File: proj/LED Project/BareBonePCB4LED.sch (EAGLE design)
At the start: 12 parts, among them J3 AVR_SPI_PROG_3X2NS, Y1 16MHz

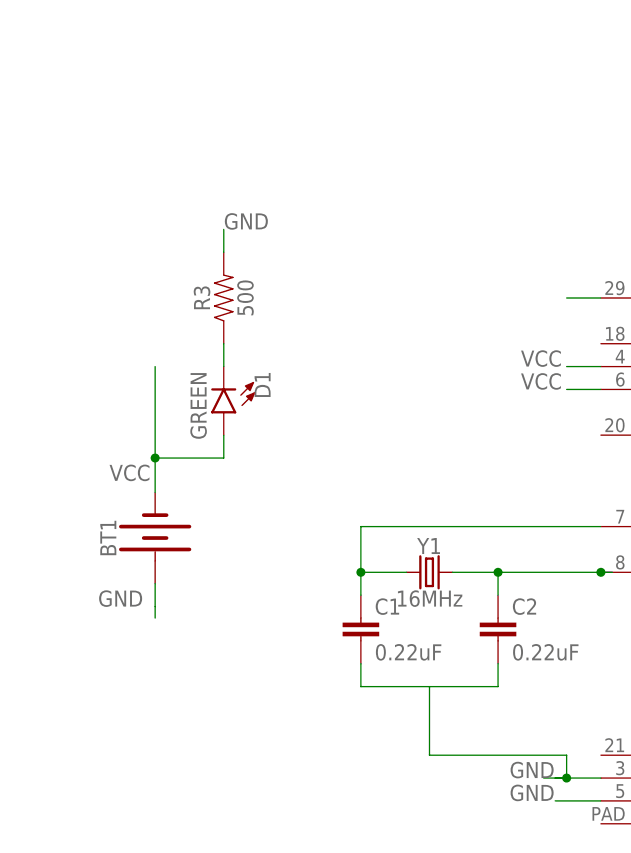
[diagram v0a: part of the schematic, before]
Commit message: Added volt regulator to bring battery from 9v to 5v for board tests
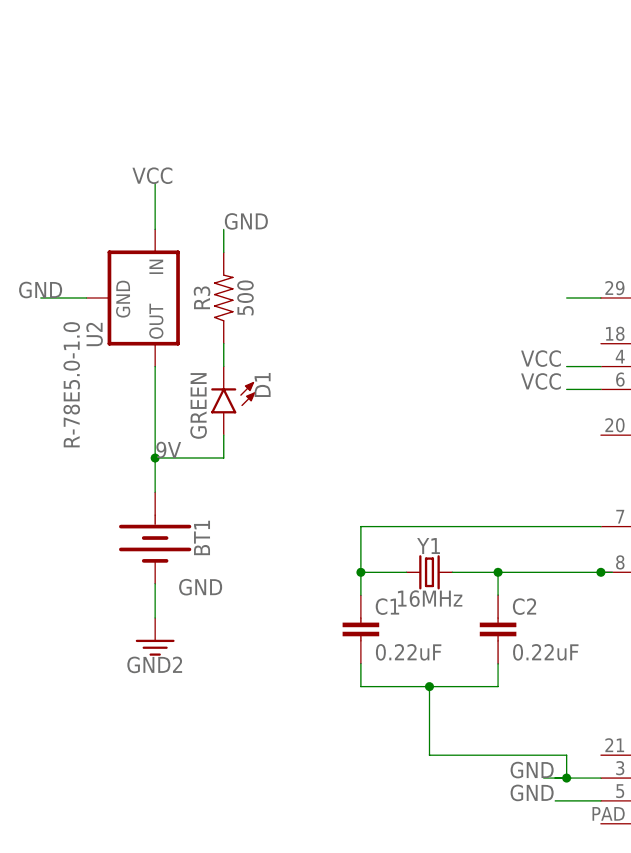
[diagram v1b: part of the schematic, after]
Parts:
- added U2: R-78E5.0-1.0, SparkFun-IC-Power:R-78E5.0-1.0
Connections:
- removed net N$15: U1.PC6(/RESET)
- new net 9V: BT1.+, D1.A, U2.OUT
- net GND: now also BT1.-, U2.GND; no longer BT1.+
- net RST: now also U1.PC6(/RESET)
- net VCC: now also U2.IN; no longer BT1.-, D1.A
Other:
- moved on the sheet: BT1
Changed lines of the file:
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@@
 <part name="C1" library="SparkFun-Capacitors" library_urn="urn:adsk.eagle:library:510" deviceset="0.22UF" device="-0603-25V-10%" package3d_urn="urn:adsk.eagle:package:37414/1" value="0.22uF"/>
 <part name="C2" library="SparkFun-Capacitors" library_urn="urn:adsk.eagle:library:510" deviceset="0.22UF" device="-0603-25V-10%" package3d_urn="urn:adsk.eagle:package:37414/1" value="0.22uF"/>
+<part name="GND" library="SparkFun-PowerSymbols" library_urn="urn:adsk.eagle:library:530" deviceset="GND2" device=""/>
+<part name="U2" library="SparkFun-IC-Power" library_urn="urn:adsk.eagle:library:526" deviceset="R-78E5.0-1.0" device="" package3d_urn="urn:adsk.eagle:package:39086/1"/>
 </parts>
 <sheets>
@@
 <instances>
 <instance part="U1" gate="U$1" x="77.47" y="55.88"/>
-<instance part="BT1" gate="G$1" x="5.08" y="54.61" rot="R90"/>
+<instance part="BT1" gate="G$1" x="5.08" y="54.61" rot="R270"/>
 <instance part="J2" gate="J$1" x="91.44" y="91.44"/>
 <instance part="J1" gate="J$1" x="91.44" y="104.14"/>
@@
 <instance part="C1" gate="G$1" x="27.94" y="43.18"/>
 <instance part="C2" gate="G$1" x="43.18" y="43.18"/>
+<instance part="GND" gate="G$1" x="5.08" y="43.18"/>
+<instance part="U2" gate="G$1" x="5.08" y="81.28" rot="R270"/>
 </instances>
 <busses>
@@
 <nets>
 <net name="GND" class="0">
-<segment>
-<pinref part="BT1" gate="G$1" pin="+"/>
-<wire x1="5.08" y1="49.53" x2="5.08" y2="46.99" width="0.1524" layer="91"/>
-<wire x1="5.08" y1="45.72" x2="5.08" y2="46.99" width="0.1524" layer="91"/>
-<label x="-1.27" y="46.99" size="1.778" layer="95"/>
-</segment>
 <segment>
 <pinref part="U1" gate="U$1" pin="GND@3"/>
@@
 <junction x="50.8" y="27.94"/>
 <wire x1="50.8" y1="27.94" x2="48.26" y2="27.94" width="0.1524" layer="91"/>
+<junction x="35.56" y="38.1"/>
 </segment>
 <segment>
@@
 <label x="12.7" y="88.9" size="1.778" layer="95"/>
 </segment>
+<segment>
+<pinref part="BT1" gate="G$1" pin="-"/>
+<wire x1="5.08" y1="49.53" x2="5.08" y2="45.72" width="0.1524" layer="91"/>
+<pinref part="GND" gate="G$1" pin="3.3V"/>
+<label x="7.62" y="48.26" size="1.778" layer="95"/>
+</segment>
+<segment>
+<pinref part="U2" gate="G$1" pin="GND"/>
+<wire x1="-2.54" y1="81.28" x2="-7.62" y2="81.28" width="0.1524" layer="91"/>
+<label x="-10.16" y="81.28" size="1.778" layer="95"/>
+</segment>
 </net>
 <net name="VCC" class="0">
@@
 </segment>
 <segment>
-<pinref part="BT1" gate="G$1" pin="-"/>
-<label x="0" y="60.96" size="1.778" layer="95"/>
-<wire x1="5.08" y1="59.69" x2="5.08" y2="63.5" width="0.1524" layer="91"/>
-<wire x1="5.08" y1="63.5" x2="5.08" y2="73.66" width="0.1524" layer="91"/>
-<wire x1="5.08" y1="63.5" x2="12.7" y2="63.5" width="0.1524" layer="91"/>
-<junction x="5.08" y="63.5"/>
-<pinref part="D1" gate="G$1" pin="A"/>
-<wire x1="12.7" y1="66.04" x2="12.7" y2="63.5" width="0.1524" layer="91"/>
-</segment>
-<segment>
 <pinref part="J3" gate="G$1" pin="2"/>
 <wire x1="147.32" y1="53.34" x2="149.86" y2="53.34" width="0.1524" layer="91"/>
 <label x="149.86" y="53.34" size="1.778" layer="95"/>
+</segment>
+<segment>
+<pinref part="U2" gate="G$1" pin="IN"/>
+<wire x1="5.08" y1="88.9" x2="5.08" y2="93.98" width="0.1524" layer="91"/>
+<label x="2.54" y="93.98" size="1.778" layer="95"/>
 </segment>
 </net>
@@
 <label x="121.92" y="48.26" size="1.778" layer="95"/>
 </segment>
+<segment>
+<pinref part="U1" gate="U$1" pin="PC6(/RESET)"/>
+<wire x1="54.61" y1="81.28" x2="50.8" y2="81.28" width="0.1524" layer="91"/>
+</segment>
 </net>
 <net name="MOSI" class="0">
@@
 <wire x1="102.87" y1="27.94" x2="106.68" y2="27.94" width="0.1524" layer="91"/>
 <label x="106.68" y="27.94" size="1.778" layer="95"/>
-</segment>
-</net>
-<net name="N$15" class="0">
-<segment>
-<pinref part="U1" gate="U$1" pin="PC6(/RESET)"/>
-<wire x1="54.61" y1="81.28" x2="50.8" y2="81.28" width="0.1524" layer="91"/>
 </segment>
 </net>
@@
 </segment>
 </net>
+<net name="9V" class="0">
+<segment>
+<label x="5.08" y="63.5" size="1.778" layer="95"/>
+<wire x1="5.08" y1="63.5" x2="5.08" y2="73.66" width="0.1524" layer="91"/>
+<wire x1="5.08" y1="63.5" x2="12.7" y2="63.5" width="0.1524" layer="91"/>
+<pinref part="D1" gate="G$1" pin="A"/>
+<wire x1="12.7" y1="66.04" x2="12.7" y2="63.5" width="0.1524" layer="91"/>
+<pinref part="BT1" gate="G$1" pin="+"/>
+<wire x1="5.08" y1="59.69" x2="5.08" y2="63.5" width="0.1524" layer="91"/>
+<junction x="5.08" y="63.5"/>
+<pinref part="U2" gate="G$1" pin="OUT"/>
+</segment>
+</net>
 </nets>
 </sheet>
 </sheets>
+<errors>
+</errors>
 </schematic>
 </drawing>

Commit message: Making the PCB pretty
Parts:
- renumbered BT1 to BAT, J1 to NP2, J2 to NP1, U2 to VR
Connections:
- removed net N$1: NP1.1, U1.PC0(ADC0)
- removed net N$3: NP1.3, U1.PC2(ADC2)
- removed net N$4: NP2.1, U1.PC3(ADC3)
- removed net N$6: NP2.3, U1.PC5(ADC5/SCL)
- net GND: now also NP1.1, NP2.1
- net VCC: now also NP1.3, NP2.3
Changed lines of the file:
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@@
 <parts>
 <part name="U1" library="SparkFun-IC-Microcontroller" library_urn="urn:adsk.eagle:library:525" deviceset="ATMEGA328P_MLF" device="MLF32" package3d_urn="urn:adsk.eagle:package:38946/1"/>
-<part name="BT1" library="SparkFun-Batteries" library_urn="urn:adsk.eagle:library:508" deviceset="BATTERY" device="-9V" package3d_urn="urn:adsk.eagle:package:37219/1"/>
-<part name="J2" library="SparkFun-Connectors" library_urn="urn:adsk.eagle:library:513" deviceset="CONN_03" device="" package3d_urn="urn:adsk.eagle:package:38063/1"/>
-<part name="J1" library="SparkFun-Connectors" library_urn="urn:adsk.eagle:library:513" deviceset="CONN_03" device="" package3d_urn="urn:adsk.eagle:package:38063/1"/>
+<part name="BAT" library="SparkFun-Batteries" library_urn="urn:adsk.eagle:library:508" deviceset="BATTERY" device="-9V" package3d_urn="urn:adsk.eagle:package:37219/1"/>
+<part name="NP1" library="SparkFun-Connectors" library_urn="urn:adsk.eagle:library:513" deviceset="CONN_03" device="" package3d_urn="urn:adsk.eagle:package:38063/1"/>
+<part name="NP2" library="SparkFun-Connectors" library_urn="urn:adsk.eagle:library:513" deviceset="CONN_03" device="" package3d_urn="urn:adsk.eagle:package:38063/1"/>
 <part name="J3" library="SparkFun-Connectors" library_urn="urn:adsk.eagle:library:513" deviceset="AVR_SPI_PROG_3X2" device="NS" package3d_urn="urn:adsk.eagle:package:38013/1"/>
 <part name="R1" library="SparkFun-Resistors" library_urn="urn:adsk.eagle:library:532" deviceset="470OHM" device="-0603-1/10W-1%" package3d_urn="urn:adsk.eagle:package:39650/1" value="470"/>
@@
 <part name="C2" library="SparkFun-Capacitors" library_urn="urn:adsk.eagle:library:510" deviceset="0.22UF" device="-0603-25V-10%" package3d_urn="urn:adsk.eagle:package:37414/1" value="0.22uF"/>
 <part name="GND" library="SparkFun-PowerSymbols" library_urn="urn:adsk.eagle:library:530" deviceset="GND2" device=""/>
-<part name="U2" library="SparkFun-IC-Power" library_urn="urn:adsk.eagle:library:526" deviceset="R-78E5.0-1.0" device="" package3d_urn="urn:adsk.eagle:package:39086/1"/>
+<part name="VR" library="SparkFun-IC-Power" library_urn="urn:adsk.eagle:library:526" deviceset="R-78E5.0-1.0" device="" package3d_urn="urn:adsk.eagle:package:39086/1"/>
 </parts>
 <sheets>
@@
 <instances>
 <instance part="U1" gate="U$1" x="77.47" y="55.88"/>
-<instance part="BT1" gate="G$1" x="5.08" y="54.61" rot="R270"/>
-<instance part="J2" gate="J$1" x="91.44" y="91.44"/>
-<instance part="J1" gate="J$1" x="91.44" y="104.14"/>
+<instance part="BAT" gate="G$1" x="5.08" y="54.61" rot="R270"/>
+<instance part="NP1" gate="J$1" x="91.44" y="91.44"/>
+<instance part="NP2" gate="J$1" x="91.44" y="104.14"/>
 <instance part="J3" gate="G$1" x="137.16" y="50.8"/>
 <instance part="R1" gate="G$1" x="104.14" y="86.36" rot="R90"/>
@@
 <instance part="C2" gate="G$1" x="43.18" y="43.18"/>
 <instance part="GND" gate="G$1" x="5.08" y="43.18"/>
-<instance part="U2" gate="G$1" x="5.08" y="81.28" rot="R270"/>
+<instance part="VR" gate="G$1" x="5.08" y="81.28" rot="R270"/>
 </instances>
 <busses>
@@
 </segment>
 <segment>
-<pinref part="BT1" gate="G$1" pin="-"/>
+<pinref part="BAT" gate="G$1" pin="-"/>
 <wire x1="5.08" y1="49.53" x2="5.08" y2="45.72" width="0.1524" layer="91"/>
 <pinref part="GND" gate="G$1" pin="3.3V"/>
@@
 </segment>
 <segment>
-<pinref part="U2" gate="G$1" pin="GND"/>
+<pinref part="VR" gate="G$1" pin="GND"/>
 <wire x1="-2.54" y1="81.28" x2="-7.62" y2="81.28" width="0.1524" layer="91"/>
 <label x="-10.16" y="81.28" size="1.778" layer="95"/>
+</segment>
+<segment>
+<pinref part="NP1" gate="J$1" pin="1"/>
+<wire x1="99.06" y1="88.9" x2="101.6" y2="88.9" width="0.1524" layer="91"/>
+<label x="99.06" y="88.9" size="1.778" layer="95"/>
+</segment>
+<segment>
+<pinref part="NP2" gate="J$1" pin="1"/>
+<wire x1="99.06" y1="101.6" x2="101.6" y2="101.6" width="0.1524" layer="91"/>
+<label x="99.06" y="101.6" size="1.778" layer="95"/>
 </segment>
 </net>
@@
 </segment>
 <segment>
-<pinref part="U2" gate="G$1" pin="IN"/>
+<pinref part="VR" gate="G$1" pin="IN"/>
 <wire x1="5.08" y1="88.9" x2="5.08" y2="93.98" width="0.1524" layer="91"/>
 <label x="2.54" y="93.98" size="1.778" layer="95"/>
 </segment>
-</net>
-<net name="N$1" class="0">
-<segment>
-<pinref part="U1" gate="U$1" pin="PC0(ADC0)"/>
-<wire x1="102.87" y1="81.28" x2="102.87" y2="88.9" width="0.1524" layer="91"/>
-<wire x1="102.87" y1="88.9" x2="99.06" y2="88.9" width="0.1524" layer="91"/>
-<pinref part="J2" gate="J$1" pin="1"/>
+<segment>
+<pinref part="NP1" gate="J$1" pin="3"/>
+<wire x1="99.06" y1="93.98" x2="101.6" y2="93.98" width="0.1524" layer="91"/>
+<label x="99.06" y="93.98" size="1.778" layer="95"/>
+</segment>
+<segment>
+<pinref part="NP2" gate="J$1" pin="3"/>
+<wire x1="99.06" y1="106.68" x2="101.6" y2="106.68" width="0.1524" layer="91"/>
+<label x="99.06" y="106.68" size="1.778" layer="95"/>
 </segment>
 </net>
@@
 <segment>
 <wire x1="104.14" y1="91.44" x2="99.06" y2="91.44" width="0.1524" layer="91"/>
-<pinref part="J2" gate="J$1" pin="2"/>
+<pinref part="NP1" gate="J$1" pin="2"/>
 <pinref part="R1" gate="G$1" pin="2"/>
 </segment>
 </net>
-<net name="N$3" class="0">
-<segment>
-<pinref part="U1" gate="U$1" pin="PC2(ADC2)"/>
-<wire x1="102.87" y1="76.2" x2="106.68" y2="76.2" width="0.1524" layer="91"/>
-<wire x1="106.68" y1="76.2" x2="106.68" y2="93.98" width="0.1524" layer="91"/>
-<pinref part="J2" gate="J$1" pin="3"/>
-<wire x1="106.68" y1="93.98" x2="99.06" y2="93.98" width="0.1524" layer="91"/>
-</segment>
-</net>
-<net name="N$4" class="0">
-<segment>
-<pinref part="U1" gate="U$1" pin="PC3(ADC3)"/>
-<wire x1="102.87" y1="73.66" x2="109.22" y2="73.66" width="0.1524" layer="91"/>
-<wire x1="109.22" y1="73.66" x2="109.22" y2="101.6" width="0.1524" layer="91"/>
-<pinref part="J1" gate="J$1" pin="1"/>
-<wire x1="109.22" y1="101.6" x2="99.06" y2="101.6" width="0.1524" layer="91"/>
-</segment>
-</net>
 <net name="N$5" class="0">
 <segment>
-<pinref part="J1" gate="J$1" pin="2"/>
+<pinref part="NP2" gate="J$1" pin="2"/>
 <wire x1="99.06" y1="104.14" x2="111.76" y2="104.14" width="0.1524" layer="91"/>
 <pinref part="R2" gate="G$1" pin="2"/>
 <wire x1="111.76" y1="93.98" x2="111.76" y2="104.14" width="0.1524" layer="91"/>
-</segment>
-</net>
-<net name="N$6" class="0">
-<segment>
-<pinref part="U1" gate="U$1" pin="PC5(ADC5/SCL)"/>
-<wire x1="102.87" y1="68.58" x2="114.3" y2="68.58" width="0.1524" layer="91"/>
-<wire x1="114.3" y1="68.58" x2="114.3" y2="106.68" width="0.1524" layer="91"/>
-<pinref part="J1" gate="J$1" pin="3"/>
-<wire x1="114.3" y1="106.68" x2="99.06" y2="106.68" width="0.1524" layer="91"/>
 </segment>
 </net>
@@
 <pinref part="D1" gate="G$1" pin="A"/>
 <wire x1="12.7" y1="66.04" x2="12.7" y2="63.5" width="0.1524" layer="91"/>
-<pinref part="BT1" gate="G$1" pin="+"/>
+<pinref part="BAT" gate="G$1" pin="+"/>
 <wire x1="5.08" y1="59.69" x2="5.08" y2="63.5" width="0.1524" layer="91"/>
 <junction x="5.08" y="63.5"/>
-<pinref part="U2" gate="G$1" pin="OUT"/>
-</segment>
-</net>
+<pinref part="VR" gate="G$1" pin="OUT"/>
+</segment>
+</net>

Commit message: fixes
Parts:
- removed BAT: (no value), SparkFun-Batteries:BATTERY-9V
- removed VR: R-78E5.0-1.0, SparkFun-IC-Power:R-78E5.0-1.0
- added BT1: (no value), SparkFun-Batteries:BATTERY-9V
- added C3: 1mF, SparkFun-Capacitors:1000UF-RADIAL-5MM-25V-20%
- added R4: 400, SparkFun-Resistors:470OHM-0603-1/10W-1%
- added S1: MOMENTARY-SWITCH-SPST-PTH-6.0MM-KIT, SparkFun-Switches:MOMENTARY-SWITCH-SPST-PTH-6.0MM-KIT
- added U2: (no value), SparkFun-IC-Microcontroller:ATMEGA328P_MLFMLF32
- R1: value 470 -> 83
- R2: value 470 -> 10k
- R3: value 500 -> 400; device SparkFun-Resistors:0.1OHM-1210-1/2W-1% -> SparkFun-Resistors:470OHM-0603-1/10W-1%
- U1: value (none) -> R-78E5.0-1.0; device SparkFun-IC-Microcontroller:ATMEGA328P_MLFMLF32 -> SparkFun-IC-Power:R-78E5.0-1.0
- renumbered NP1 to J2, NP2 to J1
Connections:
- removed net N$11: C1.1, U1.PB6(XTAL1/TOSC1), Y1.1
- removed net N$12: C2.1, U1.PB7(XTAL2/TOSC2), Y1.2
- removed net N$2: J2.2, R1.2
- removed net N$5: J1.2, R2.2
- removed net N$8: R2.1, U1.PC4(ADC4/SDA)
- new net DATA: R4.1, U2.PC4(ADC4/SDA)
- new net DATA1: J2.2, R3.2
- new net DATA2: J1.2, R4.2
- new net XTAL1: C1.1, U2.PB6(XTAL1/TOSC1), Y1.1
- new net XTAL2: C2.1, U2.PB7(XTAL2/TOSC2), Y1.2
- net 9V: now also BT1.+, U1.OUT; no longer BAT.+, D1.A, VR.OUT
- net GND: now also BT1.-, C3.-, R1.2, S1.2, U1.GND, U2.GND@3, U2.GND@5, U2.GND@PAD; no longer BAT.-, R3.2, U1.GND@3, U1.GND@5, VR.GND
- net MISO: now also U2.PB4(MISO); no longer U1.PB4(MISO)
- net MOSI: now also U2.PB3(MOSI/OC2); no longer U1.PB3(MOSI/OC2)
- net N$10: now also R1.1; no longer R3.1
- net N$7: now also R3.1, U2.PC1(ADC1); no longer R1.1, U1.PC1(ADC1)
- net RST: now also R2.2, S1.1, U2.PC6(/RESET); no longer U1.PC6(/RESET)
- net RX: now also U2.PD0(RXD); no longer U1.PD0(RXD)
- net SCK: now also U2.PB5(SCK); no longer U1.PB5(SCK)
- net TX: now also U2.PD1(TXD); no longer U1.PD1(TXD)
- net VCC: now also C3.+, D1.A, R2.1, U1.IN, U2.AVCC, U2.VCC@4, U2.VCC@6; no longer U1.VCC@4, U1.VCC@6, VR.IN
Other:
- moved on the sheet: D1, R1, R2, R3
